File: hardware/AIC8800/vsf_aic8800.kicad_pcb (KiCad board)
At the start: 2 copper layers, 27.9 x 50.8 mm, 33 parts, among them J0 USB_C_Receptacle_USB2.0, J1 Conn_01x20, J2 Conn_01x20, J3 Conn_02x05_Counter_Clockwise, Q0 AO3401, Q1 AO3402, SW0 SW_Push, SW1 SW_Push, U0 Module_AIC8800M

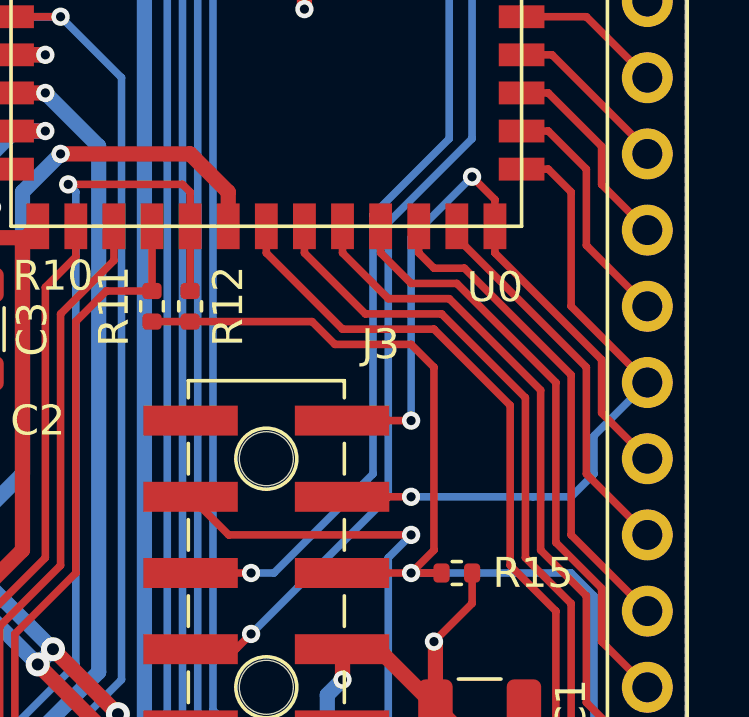
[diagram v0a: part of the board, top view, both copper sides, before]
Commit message: [hardware/aic88800] update silks
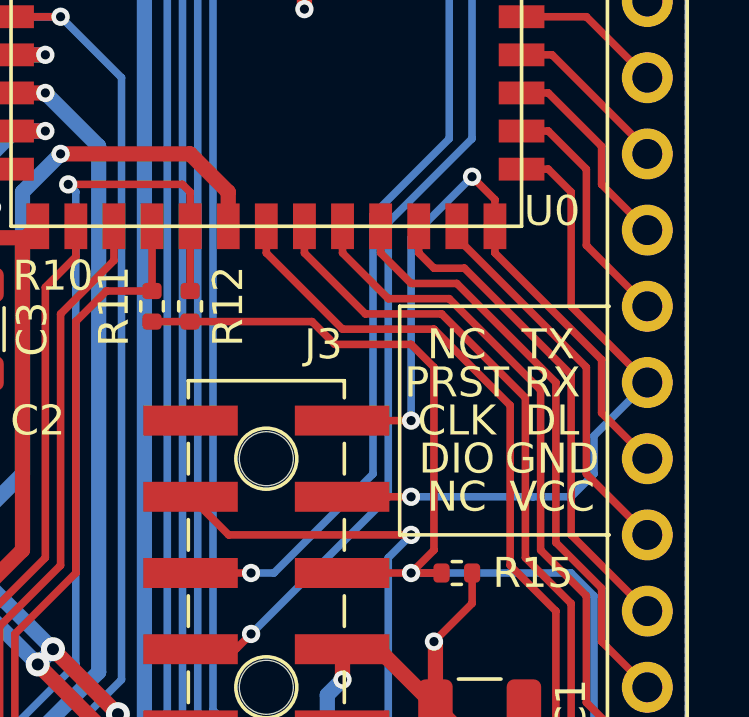
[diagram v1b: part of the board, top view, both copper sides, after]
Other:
- board text added: "CLK"
- board text added: "DIO"
- board text added: "NC"
- board text added: "RX"
- board text added: "TX"
